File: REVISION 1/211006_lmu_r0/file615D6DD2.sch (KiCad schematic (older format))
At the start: 16 parts

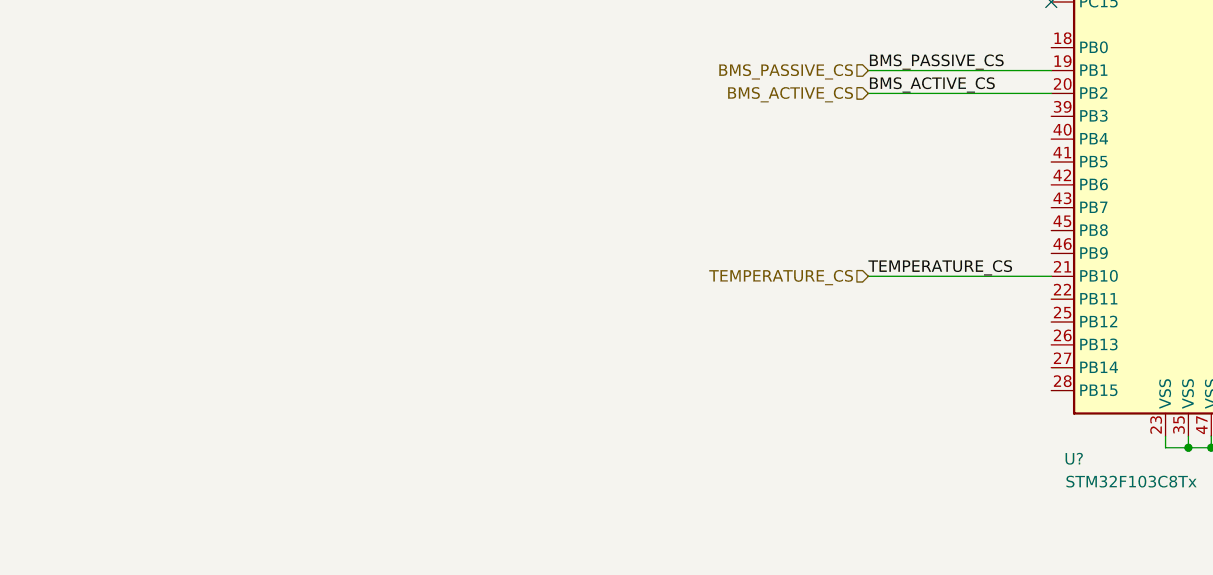
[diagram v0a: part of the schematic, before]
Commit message: Added new a-balancer interface
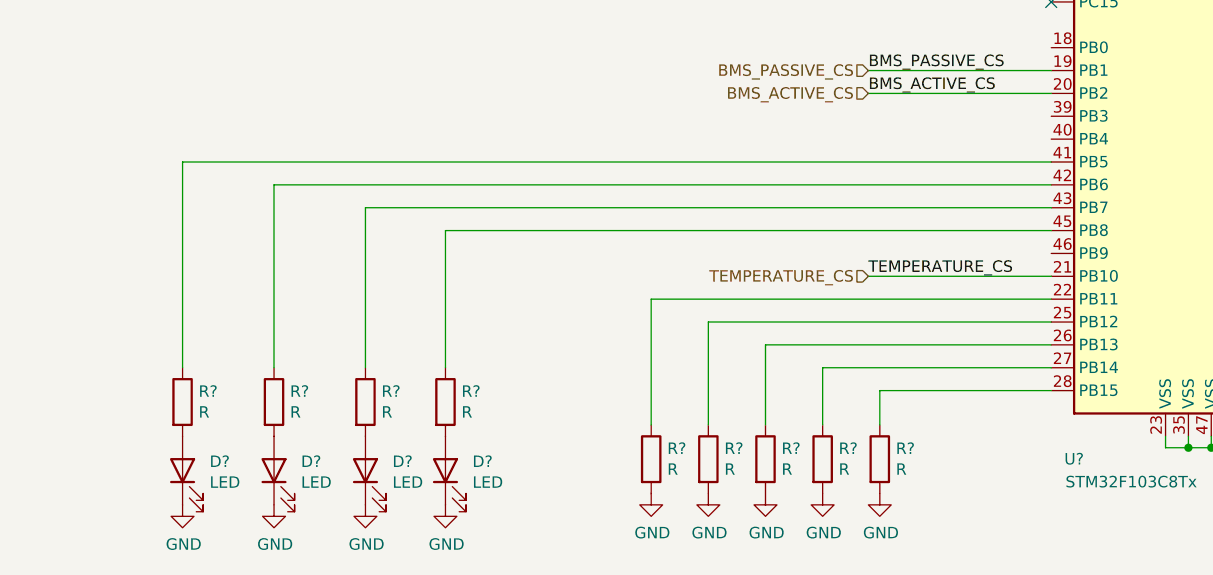
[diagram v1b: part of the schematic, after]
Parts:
- added D? (x4): LED, symbol Device:LED
- added R? (x9): R, symbol Device:R
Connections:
- wire segments 55 -> 73

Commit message: LMU design init
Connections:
- net labels added: +3V3_ISO, GND_ISO, LMS_OK_FB
- net labels removed: +3.3V, GND
- wire segments 73 -> 79
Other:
- moved on the sheet: C?

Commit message: Finished schematic, ready for pcb layout
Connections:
- net labels added: CS_ACTIVE_LOWER, CS_ACTIVE_UPPER, CS_PASSIVE, CS_TEMPERATURE, WDT_ACTIVE_LOWER, WDT_ACTIVE_UPPER, WDT_PASSIVE
- net labels removed: BMS_ACTIVE_CS, BMS_PASSIVE_CS
- wire segments 79 -> 84
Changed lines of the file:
@@
 $Descr A4 11693 8268
 encoding utf-8
-Sheet 3 30
+Sheet 35 35
 Title ""
 Date ""
@@
 Text HLabel 7400 4400 2    50   Input ~ 0
 SPI1_MOSI
-Text Label 4800 3800 0    50   ~ 0
-BMS_PASSIVE_CS
-Text Label 4800 3900 0    50   ~ 0
-BMS_ACTIVE_CS
 Text Label 4800 4700 0    50   ~ 0
 TEMPERATURE_CS
 Wire Wire Line
 	4800 4700 5600 4700
-Wire Wire Line
-	4800 3900 5600 3900
-Wire Wire Line
-	5600 3800 4800 3800
 Wire Wire Line
 	1250 2050 1350 2050
@@
 	1    0    0    -1
 $EndComp
-Text HLabel 4800 3800 0    50   Input ~ 0
-BMS_PASSIVE_CS
-Text HLabel 4800 3900 0    50   Input ~ 0
-BMS_ACTIVE_CS
-Text HLabel 4800 4700 0    50   Input ~ 0
-TEMPERATURE_CS
 Text Label 7100 4600 0    50   ~ 0
 LMS_OK
@@
 Wire Wire Line
 	1800 4200 1800 5100
-Text HLabel 7400 4500 2    50   Input ~ 0
-LMS_OK_FB
 Wire Wire Line
 	7400 4500 6900 4500
@@
 	1    0    0    -1
 $EndComp
+Text HLabel 5450 3700 0    50   Input ~ 0
+CS_ACTIVE_UPPER
+Text HLabel 5450 3800 0    50   Input ~ 0
+WDT_ACTIVE_UPPER
+Text HLabel 7400 4100 2    50   Input ~ 0
+WDT_PASSIVE
+Text HLabel 7400 3700 2    50   Input ~ 0
+CS_TEMPERATURE
+Text HLabel 7400 3800 2    50   Input ~ 0
+CS_PASSIVE
+Text HLabel 7400 4500 2    50   Input ~ 0
+LMS_OK_FB
+Text HLabel 5450 3900 0    50   Input ~ 0
+CS_ACTIVE_LOWER
+Text HLabel 5450 4000 0    50   Input ~ 0
+WDT_ACTIVE_LOWER
+Wire Wire Line
+	7400 3700 6900 3700
+Wire Wire Line
+	6900 3800 7400 3800
+Wire Wire Line
+	7400 4100 6900 4100
+Wire Wire Line
+	5450 3700 5600 3700
+Wire Wire Line
+	5450 3800 5600 3800
+Wire Wire Line
+	5450 3900 5600 3900
+Wire Wire Line
+	5450 4000 5600 4000
 $EndSCHEMATC
